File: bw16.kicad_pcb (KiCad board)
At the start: 2 copper layers, 30.8 x 57 mm, 25 parts, among them J1 Conn_01x08_Male, J2 Conn_01x08_Male, J6 +3V3, J7 GND, J8 VIN, J9 Conn_01x06_Male, M1 BW16, SW1 RESET, SW2 BURN, U1 AP1117-33

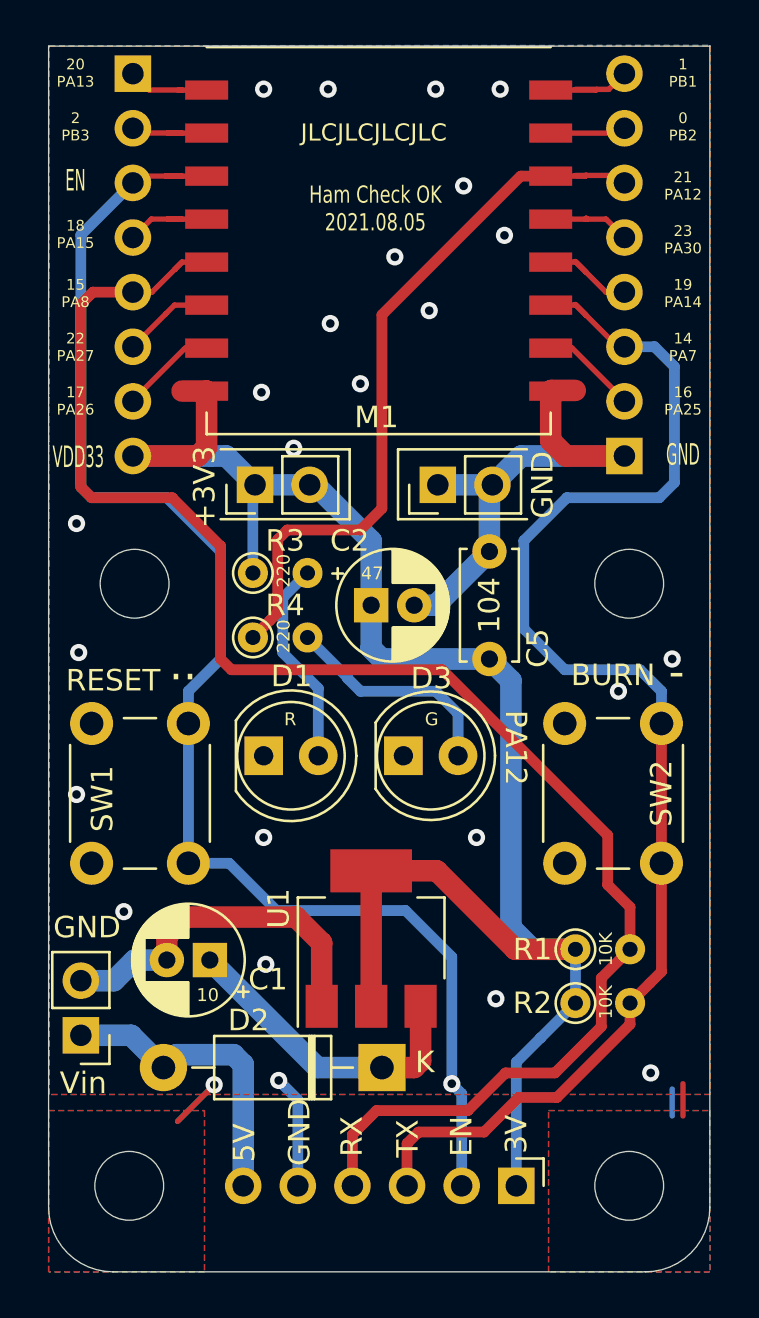
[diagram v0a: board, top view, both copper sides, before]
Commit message: Add files via upload
1.整理本地零件庫 bw16.kicad_mod
2.加入qrcode測試。qrcode來源 http://qr.calm9.com/tw/ 尺寸:L 密度:1
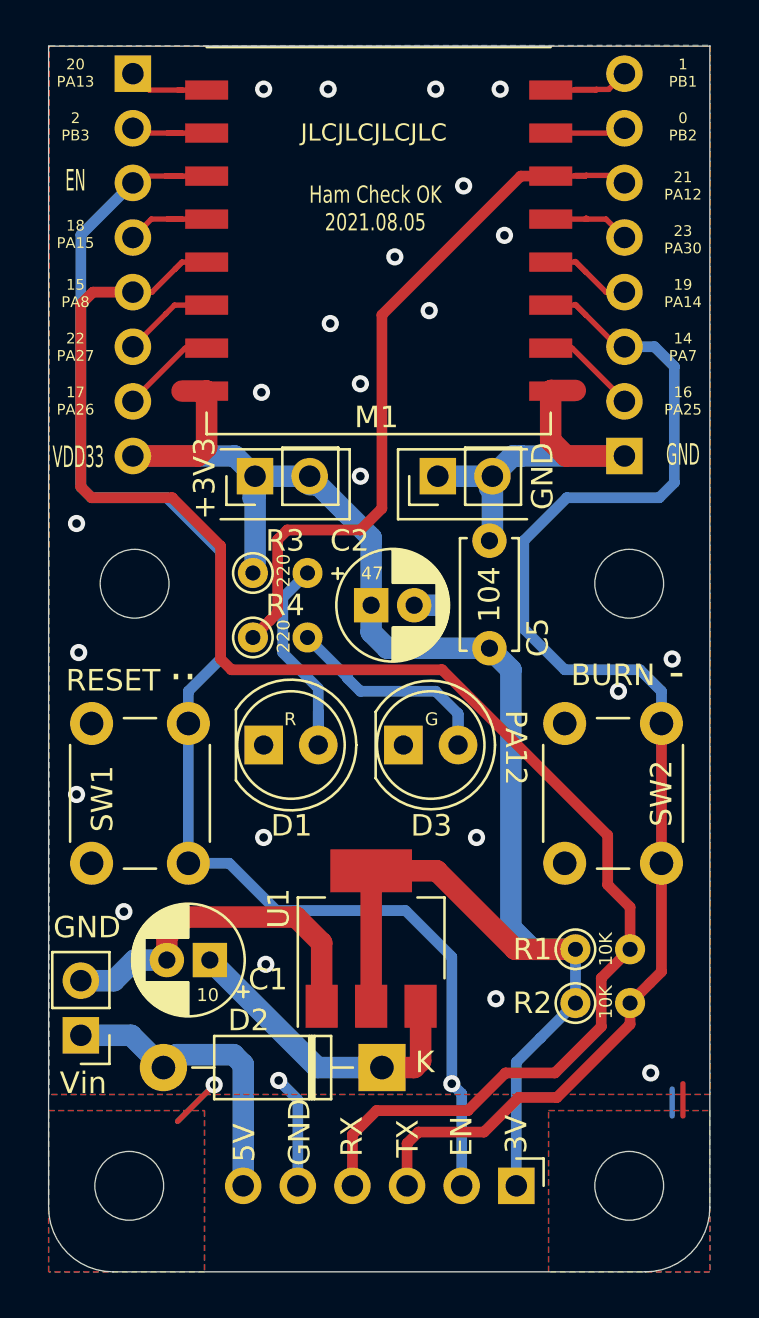
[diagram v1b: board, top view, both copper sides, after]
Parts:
- added G2: qrcode, pcb:Untitled, B.Cu at (133.5, 120.0)
- G1: renamed from G***; footprint pcb:Untitled -> bw16:accomdemy
- moved C5 0.50 mm to (138.5, 108.0)
- moved D1 0.50 mm to (128.0, 112.5)
- moved D3 0.50 mm to (134.5, 112.5)
- moved J6 0.40 mm to (127.6, 100.0)
- moved J7 0.40 mm to (136.1, 100.0)
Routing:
- net /VDD33: track 80.0 -> 85.8 mm
- net /GND: track 53.5 -> 50.3 mm
- net Net-(D1-Pad2): track 9.66 -> 10.2 mm

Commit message: Add files via upload
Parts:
- added TP1: TestPoint, TestPoint:TestPoint_Pad_1.0x1.0mm, B.Cu at (136.8, 129.7)
- added TP2: TestPoint, TestPoint:TestPoint_Pad_1.0x1.0mm, B.Cu at (138.4, 129.7)
- moved G1 0.30 mm to (133.0, 90.7)
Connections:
- J9 pad 1: /VDD33 -> Net-(J9-Pad1)
- J9 pad 2: /EN -> /LOG_TX
- J9 pad 3: /LOG_TX -> /LOG_RX
- J9 pad 4: /LOG_RX -> /VIN
- J9 pad 5: /GND -> Net-(J9-Pad5)
- J9 pad 6: /VIN -> /GND
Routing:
- net /VDD33: track 85.8 -> 80.1 mm
- net Net-(J9-Pad1): track 0.00 -> 4.50 mm
- net /EN: track 67.5 -> 64.0 mm, vias 1 -> 0
- net /LOG_RX: track 75.8 -> 72.6 mm
- net /VIN: track 14.3 -> 16.9 mm
- net /LOG_TX: track 63.6 -> 61.2 mm
- net /GND: track 50.3 -> 50.6 mm, vias 25 -> 24
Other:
- board text removed: "3V"

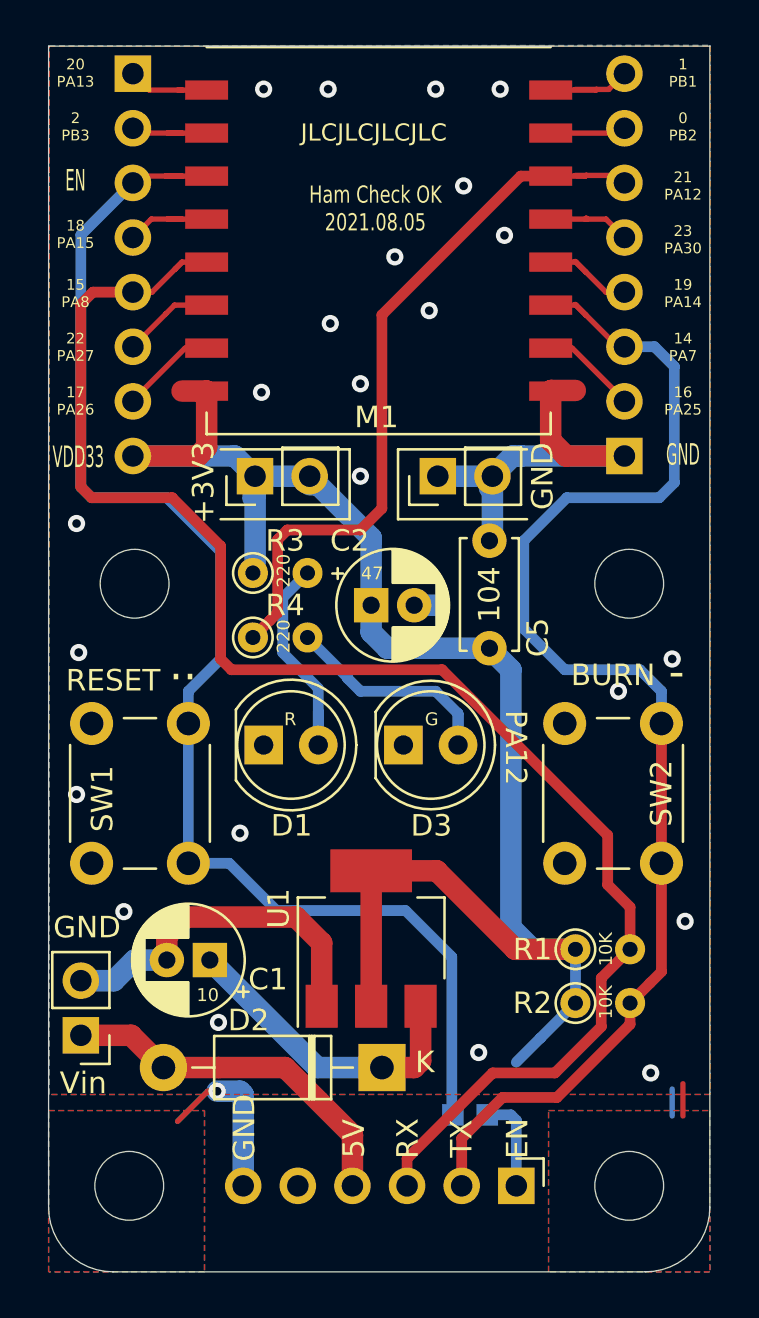
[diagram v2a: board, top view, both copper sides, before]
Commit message: 修改娟印層文字
把接腳的arduino數字拿掉
字大小與線條粗細改成JLC的建議值
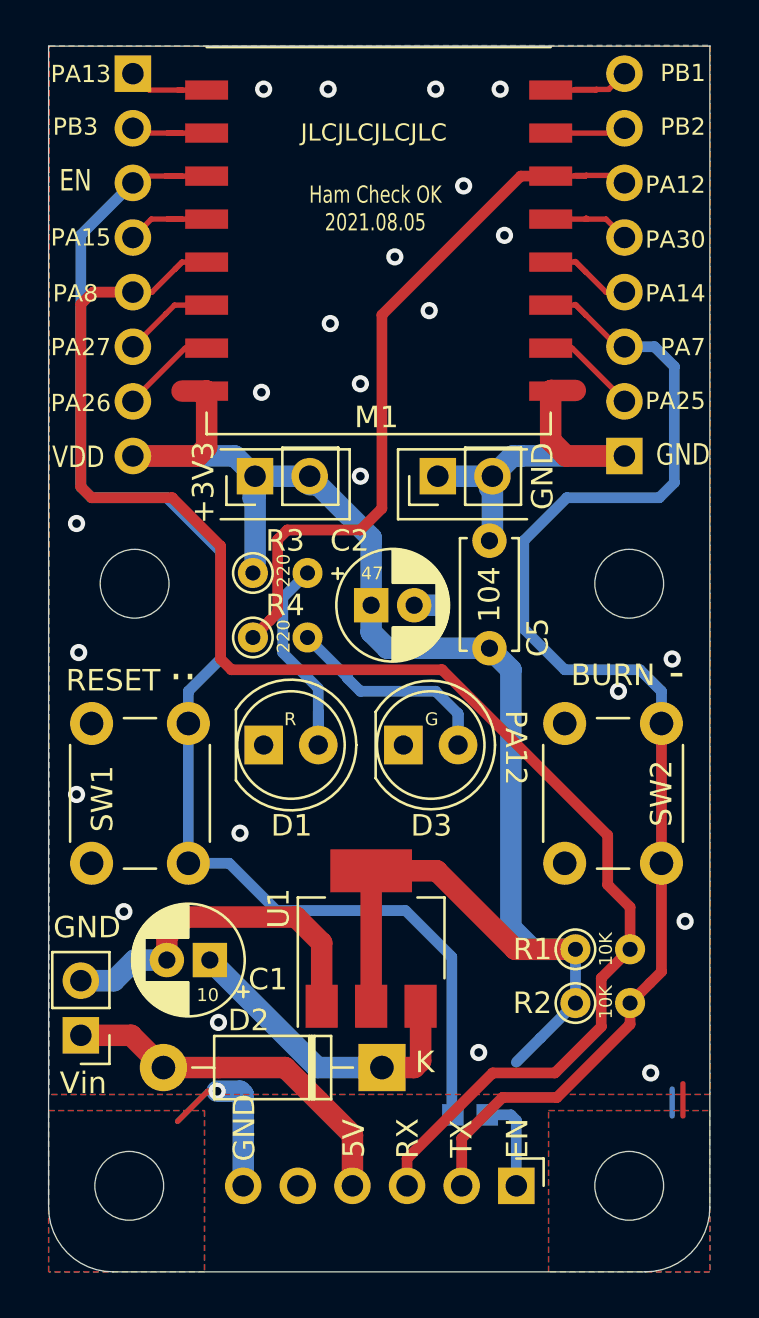
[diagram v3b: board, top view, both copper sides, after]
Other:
- board text added: "PA13"
- board text added: "PA14"
- board text added: "PA15"
- board text added: "PA25"
- board text added: "PA26"
- board text added: "PA27"
- board text added: "PA30"
- board text added: "PA7"
- board text added: "PA8"
- board text added: "PB1"
- board text added: "PB2"
- board text added: "PB3"
- board text added: "VDD"
- board text removed: "0 PB2"
- board text removed: "1 PB1"
- board text removed: "14 PA7"
- board text removed: "15 PA8"
- board text removed: "16 PA25"
- board text removed: "17 PA26"
- board text removed: "18 PA15"
- board text removed: "19 PA14"
- board text removed: "2 PB3"
- board text removed: "20 PA13"
- board text removed: "21 PA12"
- board text removed: "22 PA27"
- board text removed: "23 PA30"
- board text removed: "VDD33"

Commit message: Add files via upload
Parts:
- removed G2: qrcode, pcb:Untitled
- removed H1, H2, H3: MountingHole, MountingHole:MountingHole_3.2mm_M3
- J6: value +3V3 -> 3V3
- moved R2 17.0 mm to (125.6, 122.4), turned to 180 degrees
- moved D3 12.5 mm to (144.7, 105.3), turned to 180 degrees
- moved D1 9.25 mm to (122.2, 105.3)
- moved C1 8.70 mm to (134.2, 122.4)
- moved J8 6.93 mm to (123.3, 131.8), turned to 0 degrees
- moved U1 6.61 mm to (133.4, 114.9)
- moved D2 5.01 mm to (138.5, 127.2)
- moved SW1 2.50 mm to (122.5, 118.1)
- moved SW2 2.00 mm to (140.0, 118.1)
- moved H4 1.94 mm to (143.4, 134.1)
- moved R1 1.84 mm to (140.7, 122.4)
- moved R3 1.03 mm to (128.0, 103.6)
- moved R4 1.03 mm to (128.0, 108.4)
- moved C5 0.32 mm to (138.6, 108.3)
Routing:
- net /EN: track 64.0 -> 93.0 mm
- net /GND: track 50.6 -> 27.0 mm, vias 24 -> 21
- net /LOG_TX: track 61.2 -> 78.0 mm
- net /LOG_RX: track 72.6 -> 63.6 mm
- net /VDD33: track 80.1 -> 73.9 mm
- net Net-(D1-Pad2): track 10.2 -> 6.50 mm
- net /VIN: track 16.9 -> 14.3 mm
- net Net-(C1-Pad1): track 14.5 -> 12.3 mm
- net Net-(D3-Pad2): track 10.9 -> 12.9 mm
- net /PA12: track 34.1 -> 33.5 mm
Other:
- board size 30.8 x 57 mm -> 25.2 x 57 mm
- board text added: "10u"
- board text added: "47u"
- board text added: "A 12"
- board text added: "A 13"
- board text added: "A 14"
- board text added: "A 15"
- board text added: "A 25"
- board text added: "A 26"
- board text added: "A 27"
- board text added: "A 30"
- board text added: "A12"
- board text added: "A7"
- board text added: "A8"
- board text added: "B1"
- board text added: "B2"
- board text added: "B3"
- board text added: "Ham Check OK 2021.08.05 DaHai 2021.09.21"
- board text removed: "10"
- board text removed: "47"
- board text removed: "Ham Check OK 2021.08.05"
- board text removed: "PA12"
- board text removed: "PA13"
- board text removed: "PA14"
- board text removed: "PA15"
- board text removed: "PA25"
- board text removed: "PA26"
- board text removed: "PA27"
- board text removed: "PA30"
- board text removed: "PA7"
- board text removed: "PA8"
- board text removed: "PB1"
- board text removed: "PB2"
- board text removed: "PB3"
